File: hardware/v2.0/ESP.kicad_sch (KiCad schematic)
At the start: 33 parts, among them J11 USB_C_Receptacle_USB2.0, J8 USB_C_Receptacle_USB2.0, Q1 Q_NPN_BEC, Q2 Q_NPN_BEC, U1 AMS1117-3.3, U2 CP2102N-A01-GQFN28, U3 ESP32-S3-WROOM

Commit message: Secondary button cross
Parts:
- added BOOT1: button, my_library:Tactile_switch, symbol Switch:SW_Push
- added C29: 1u, Capacitor_SMD:C_0402_1005Metric, symbol Device:C
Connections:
- net GND: now also BOOT1.2, C29.2
- net IO00-PU: now also BOOT1.1, C29.1
- net D+_UART: now reaches J11.A6 (D+), J11.B6 (D+), U2.4 (D+)
- net D-_UART: now reaches J11.A7 (D-), J11.B7 (D-), U2.5 (D-)
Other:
- moved on the sheet: C26, C27, C28, R27, R28, R29, R30, R31, RESET1, U3

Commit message: SD karta and factory files
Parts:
- removed C22, C23: 10u, Capacitor_SMD:C_0402_1005Metric, symbol Device:C
- added C127, C128: 10uF, Capacitor_SMD:C_0603_1608Metric, symbol Device:C
- C24, C27: value 10u -> 10uF; footprint Capacitor_SMD:C_0402_1005Metric -> Capacitor_SMD:C_0603_1608Metric; LCSC C15525 -> C96446
- J11, J8: JLCPCB_CORRECTION 1.8;-0.5;180 -> 0;-1;0
- U3: JLCPCB_CORRECTION (none) -> 0;9;0; LCSC C3013946 -> C2913199
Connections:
- net 3V3: now also C128.1
- net 5V: now also C127.1
- net GND: now also C127.2, C128.2
- net IO00-PU: now also Q1.3 (C); no longer Q1.2 (E)
- net at R26.2, U2.28 (~{DTR}): now also Q1.2 (E); no longer Q1.3 (C)
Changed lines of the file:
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@@
     (effects (font (size 1.27 1.27)) (justify left))
-  )
-  (symbol (lib_id "Device:C") (at 71.12 161.29 0) (unit 1)
-    (in_bom yes) (on_board yes)
-    (property "Reference" "C23" (id 0) (at 74.041 160.1216 0)
-      (effects (font (size 1.27 1.27)) (justify left))
-    )
-    (property "Value" "10u" (id 1) (at 74.041 162.433 0)
-      (effects (font (size 1.27 1.27)) (justify left))
-    )
-    (property "Footprint" "Capacitor_SMD:C_0402_1005Metric" (id 2) (at 72.0852 165.1 0)
-      (effects (font (size 1.27 1.27)) hide)
-    )
-    (property "Datasheet" "~" (id 3) (at 71.12 161.29 0)
-      (effects (font (size 1.27 1.27)) hide)
-    )
-    (property "LCSC" "C15525" (id 4) (at 71.12 161.29 0)
-      (effects (font (size 1.27 1.27)) hide)
-    )
-    (property "JLCPCB_CORRECTION" "0;0;0" (id 5) (at 71.12 161.29 0)
-      (effects (font (size 1.27 1.27)) hide)
-    )
-    (pin "1")
-    (pin "2")
   )
   (symbol (lib_id "power:PWR_FLAG") (at 60.96 165.1 270) (unit 1)
@@
     )
     (property "JLCPCB_CORRECTION" "0;0;0" (id 5) (at 224.79 92.71 0)
+      (effects (font (size 1.27 1.27)) hide)
+    )
+    (pin "1")
+    (pin "2")
+  )
+  (symbol (lib_id "Device:C") (at 71.12 161.29 0) (unit 1)
+    (in_bom yes) (on_board yes)
+    (property "Reference" "C128" (id 0) (at 76.2 162.56 0))
+    (property "Value" "10uF" (id 1) (at 76.2 160.2486 0))
+    (property "Footprint" "Capacitor_SMD:C_0603_1608Metric" (id 2) (at 72.0852 165.1 0)
+      (effects (font (size 1.27 1.27)) hide)
+    )
+    (property "Datasheet" "~" (id 3) (at 71.12 161.29 0)
+      (effects (font (size 1.27 1.27)) hide)
+    )
+    (property "LCSC" "C96446" (id 4) (at 71.12 161.29 0)
+      (effects (font (size 1.27 1.27)) hide)
+    )
+    (property "JLCPCB_CORRECTION" "0;0;0" (id 5) (at 71.12 161.29 0)
       (effects (font (size 1.27 1.27)) hide)
     )
@@
     (pin "2")
   )
-  (symbol (lib_id "Device:C") (at 121.92 74.93 270) (unit 1)
-    (in_bom yes) (on_board yes)
-    (property "Reference" "C24" (id 0) (at 121.92 68.5292 90))
-    (property "Value" "10u" (id 1) (at 121.92 70.8406 90))
-    (property "Footprint" "Capacitor_SMD:C_0402_1005Metric" (id 2) (at 118.11 75.8952 0)
-      (effects (font (size 1.27 1.27)) hide)
-    )
-    (property "Datasheet" "~" (id 3) (at 121.92 74.93 0)
-      (effects (font (size 1.27 1.27)) hide)
-    )
-    (property "LCSC" "C15525" (id 4) (at 121.92 74.93 0)
-      (effects (font (size 1.27 1.27)) hide)
-    )
-    (property "JLCPCB_CORRECTION" "0;0;0" (id 5) (at 121.92 74.93 0)
-      (effects (font (size 1.27 1.27)) hide)
-    )
-    (pin "1")
-    (pin "2")
-  )
   (symbol (lib_id "Device:R") (at 69.85 101.6 270) (unit 1)
     (in_bom yes) (on_board yes)
@@
     )
     (property "JLCPCB_CORRECTION" "0;0;0" (id 5) (at 132.08 132.08 0)
+      (effects (font (size 1.27 1.27)) hide)
+    )
+    (pin "1")
+    (pin "2")
+  )
+  (symbol (lib_id "Device:C") (at 45.72 161.29 0) (unit 1)
+    (in_bom yes) (on_board yes)
+    (property "Reference" "C127" (id 0) (at 40.64 162.56 0))
+    (property "Value" "10uF" (id 1) (at 40.64 160.2486 0))
+    (property "Footprint" "Capacitor_SMD:C_0603_1608Metric" (id 2) (at 46.6852 165.1 0)
+      (effects (font (size 1.27 1.27)) hide)
+    )
+    (property "Datasheet" "~" (id 3) (at 45.72 161.29 0)
+      (effects (font (size 1.27 1.27)) hide)
+    )
+    (property "LCSC" "C96446" (id 4) (at 45.72 161.29 0)
+      (effects (font (size 1.27 1.27)) hide)
+    )
+    (property "JLCPCB_CORRECTION" "0;0;0" (id 5) (at 45.72 161.29 0)
+      (effects (font (size 1.27 1.27)) hide)
+    )
+    (pin "1")
+    (pin "2")
+  )
+  (symbol (lib_id "Device:C") (at 121.92 74.93 270) (unit 1)
+    (in_bom yes) (on_board yes)
+    (property "Reference" "C24" (id 0) (at 121.92 68.5292 90))
+    (property "Value" "10uF" (id 1) (at 121.92 70.8406 90))
+    (property "Footprint" "Capacitor_SMD:C_0603_1608Metric" (id 2) (at 118.11 75.8952 0)
+      (effects (font (size 1.27 1.27)) hide)
+    )
+    (property "Datasheet" "~" (id 3) (at 121.92 74.93 0)
+      (effects (font (size 1.27 1.27)) hide)
+    )
+    (property "LCSC" "C96446" (id 4) (at 121.92 74.93 0)
+      (effects (font (size 1.27 1.27)) hide)
+    )
+    (property "JLCPCB_CORRECTION" "0;0;0" (id 5) (at 121.92 74.93 0)
       (effects (font (size 1.27 1.27)) hide)
     )
@@
       (effects (font (size 1.27 1.27)) hide)
     )
-    (property "LCSC" "C3013946" (id 4) (at 250.19 43.18 0)
+    (property "LCSC" "C2913199" (id 4) (at 250.19 43.18 0)
+      (effects (font (size 1.27 1.27)) hide)
+    )
+    (property "JLCPCB_CORRECTION" "0;9;0" (id 5) (at 250.19 55.88 0)
       (effects (font (size 1.27 1.27)) hide)
     )
@@
     (in_bom yes) (on_board yes)
     (property "Reference" "C27" (id 0) (at 245.11 31.6992 90))
-    (property "Value" "10u" (id 1) (at 245.11 34.0106 90))
-    (property "Footprint" "Capacitor_SMD:C_0402_1005Metric" (id 2) (at 241.3 39.0652 0)
+    (property "Value" "10uF" (id 1) (at 245.11 34.0106 90))
+    (property "Footprint" "Capacitor_SMD:C_0603_1608Metric" (id 2) (at 241.3 39.0652 0)
       (effects (font (size 1.27 1.27)) hide)
     )
@@
       (effects (font (size 1.27 1.27)) hide)
     )
-    (property "LCSC" "C15525" (id 4) (at 245.11 38.1 0)
+    (property "LCSC" "C96446" (id 4) (at 245.11 38.1 0)
       (effects (font (size 1.27 1.27)) hide)
     )
@@
     (pin "1")
   )
-  (symbol (lib_id "Device:Q_NPN_BEC") (at 152.4 93.98 0) (mirror x) (unit 1)
-    (in_bom yes) (on_board yes)
-    (property "Reference" "Q1" (id 0) (at 157.2514 92.8116 0)
-      (effects (font (size 1.27 1.27)) (justify left))
-    )
-    (property "Value" "Q_NPN_BEC" (id 1) (at 157.2514 95.123 0)
-      (effects (font (size 1.27 1.27)) (justify left))
-    )
-    (property "Footprint" "Package_TO_SOT_SMD:SOT-23" (id 2) (at 157.48 96.52 0)
+  (symbol (lib_id "Device:Q_NPN_BEC") (at 152.4 93.98 0) (unit 1)
+    (in_bom yes) (on_board yes)
+    (property "Reference" "Q1" (id 0) (at 157.2514 95.1484 0)
+      (effects (font (size 1.27 1.27)) (justify left))
+    )
+    (property "Value" "Q_NPN_BEC" (id 1) (at 157.2514 92.837 0)
+      (effects (font (size 1.27 1.27)) (justify left))
+    )
+    (property "Footprint" "Package_TO_SOT_SMD:SOT-23" (id 2) (at 157.48 91.44 0)
       (effects (font (size 1.27 1.27)) hide)
     )
@@
     )
     (property "JLCPCB_CORRECTION" "0;0;0" (id 5) (at 193.04 92.71 0)
-      (effects (font (size 1.27 1.27)) hide)
-    )
-    (pin "1")
-    (pin "2")
-  )
-  (symbol (lib_id "Device:C") (at 45.72 161.29 0) (unit 1)
-    (in_bom yes) (on_board yes)
-    (property "Reference" "C22" (id 0) (at 48.641 160.1216 0)
-      (effects (font (size 1.27 1.27)) (justify left))
-    )
-    (property "Value" "10u" (id 1) (at 48.641 162.433 0)
-      (effects (font (size 1.27 1.27)) (justify left))
-    )
-    (property "Footprint" "Capacitor_SMD:C_0402_1005Metric" (id 2) (at 46.6852 165.1 0)
-      (effects (font (size 1.27 1.27)) hide)
-    )
-    (property "Datasheet" "~" (id 3) (at 45.72 161.29 0)
-      (effects (font (size 1.27 1.27)) hide)
-    )
-    (property "LCSC" "C15525" (id 4) (at 45.72 161.29 0)
-      (effects (font (size 1.27 1.27)) hide)
-    )
-    (property "JLCPCB_CORRECTION" "0;0;0" (id 5) (at 45.72 161.29 0)
       (effects (font (size 1.27 1.27)) hide)
     )
@@
       (effects (font (size 1.27 1.27)) hide)
     )
-    (property "JLCPCB_CORRECTION" "1.8;-0.5;180" (id 5) (at 48.26 50.8 0)
+    (property "JLCPCB_CORRECTION" "0;-1;0" (id 5) (at 48.26 50.8 0)
       (effects (font (size 1.27 1.27)) hide)
     )
@@
       (effects (font (size 1.27 1.27)) hide)
     )
-    (property "JLCPCB_CORRECTION" "1.8;-0.5;180" (id 5) (at 48.26 109.22 0)
-      (effects (font (size 1.27 1.27)) hide)
-    )
+    (property "JLCPCB_CORRECTION" "0;-1;0" (id 5) (at 48.26 109.22 0)
+      (effects (font (size 1.27 1.27)) hide)
+    )

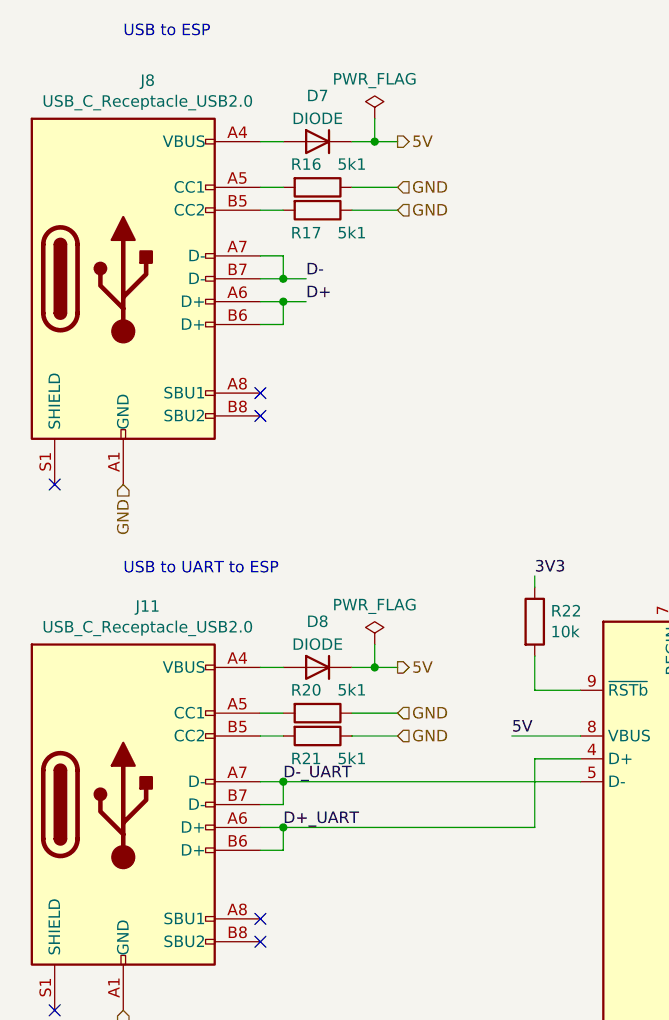
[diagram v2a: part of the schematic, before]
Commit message: Microphone and a few minor changes
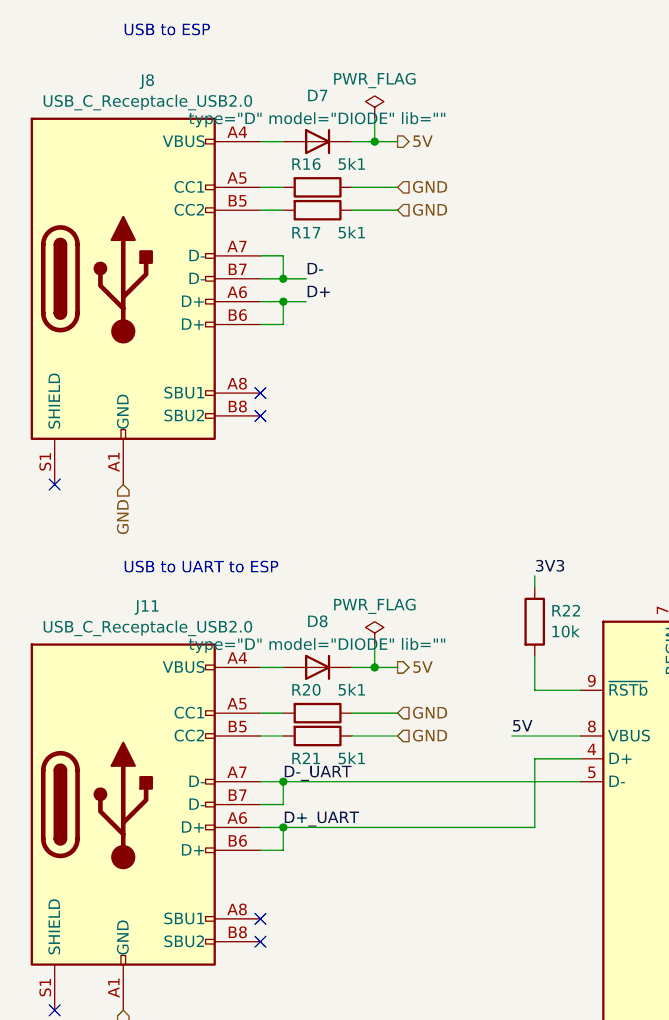
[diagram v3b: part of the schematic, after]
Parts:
- D7, D8: value DIODE -> ${SIM.PARAMS}; Spice_Netlist_Enabled Y -> (none); Spice_Primitive D -> (none)

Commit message: Small tidy up
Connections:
- net GND: now also J11.S1 (SHIELD), J8.S1 (SHIELD)
- no-connect marks 20 -> 18
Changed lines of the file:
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@@
   (no_connect (at 124.46 91.44))
   (no_connect (at 124.46 144.78))
-  (no_connect (at 40.64 132.08))
   (no_connect (at 124.46 124.46))
   (no_connect (at 124.46 139.7))
   (no_connect (at 63.5 66.04))
   (no_connect (at 63.5 124.46))
-  (no_connect (at 40.64 73.66))
   (no_connect (at 124.46 106.68))
   (no_connect (at 124.46 137.16))
@@
     (effects (font (size 1.27 1.27)) (justify left))
   )
+  (hierarchical_label "GND" (shape input) (at 40.64 73.66 270) (fields_autoplaced)
+    (effects (font (size 1.27 1.27)) (justify right))
+  )
   (hierarchical_label "IO18" (shape bidirectional) (at 261.62 101.6 0) (fields_autoplaced)
     (effects (font (size 1.27 1.27)) (justify left))
@@
     (effects (font (size 1.27 1.27)) (justify left))
   )
+  (hierarchical_label "GND" (shape input) (at 40.64 132.08 270) (fields_autoplaced)
+    (effects (font (size 1.27 1.27)) (justify right))
+  )
   (hierarchical_label "GND" (shape input) (at 111.76 152.4 270) (fields_autoplaced)
